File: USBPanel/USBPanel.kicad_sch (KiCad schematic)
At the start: 62 parts, among them J1 PORT1, J2 PORT2, J3 PWR, J4 USB_UFP, J5 SINK, J6 I2Ct, J7 I2Cc, Q1 ISZ0702NLS, Q2 ISZ0702NLS, Q3 NX138BK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

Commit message: USBPanel layout
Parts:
- added R18, R19: 4.7kΩ, Resistor_SMD:R_0603_1608Metric, symbol Device:R_US
- J7: symbol Connector_Generic:Conn_02x03_Top_Bottom -> Connector_Generic:Conn_02x03_Odd_Even
- R1, R2: value 2.2kΩ -> 4.7kΩ
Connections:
- net +3.3V: now also R18.1, R19.1
- net GND: now also J7.5 (Pin_5); no longer J7.3 (Pin_3)
- net PORT1_D+: now also U2.4 (I/O3); no longer U2.6 (I/O4)
- net PORT1_D-: now also U2.6 (I/O4); no longer U2.4 (I/O3)
- net at R1.1, U1.15 (I2Cc_SDA): now also J7.3 (Pin_3); no longer J7.5 (Pin_5)
- net at U3.5 (SDA): now also J7.4 (Pin_4), R19.2; no longer J7.2 (Pin_2)
- net at U3.6 (SCL): now also J7.2 (Pin_2), R18.2; no longer J7.1 (Pin_1)
- net at R2.1, U1.16 (I2Cc_SCL): now also J7.1 (Pin_1); no longer J7.4 (Pin_4)
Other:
- note added: "Jumper 1-2 and 3-4 for EEPROM patch loading"
- note removed: "Jumper 1-4 and 2-5 for EEPROM patch loading"

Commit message: USBPanel PCB complete
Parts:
- added C18: 10μF 50V, Capacitor_SMD:C_1206_3216Metric, symbol Device:C_Small
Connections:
- net GND: now also C18.2
- net PORT2_VBUS: now reaches C12.2, C13.2, D1.1 (A1), J2.A4 (VBUS), J2.A9 (VBUS), J2.B4 (VBUS), J2.B9 (VBUS), TP5.1, U4.14 (OUT), U4.15 (OUT)
- net PORT1_VBUS: now reaches C7.1, C8.1, J1.A4 (VBUS), J1.A9 (VBUS), J1.B4 (VBUS), J1.B9 (VBUS), Q1.1 (S), TP4.1, U1.26 (VBUS), U1.27 (VBUS), U2.5 (VBUS)
- net at J5.1 (Pin_1), Q2.1 (S), TP6.1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: now also C18.1
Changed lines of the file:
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@@
 	(wire
 		(pts
+			(xy 153.67 24.13) (xy 154.94 24.13)
+		)
+		(stroke
+			(width 0)
+			(type default)
+		)
+	)
+	(wire
+		(pts
 			(xy 233.68 52.07) (xy 264.16 52.07)
 		)
@@
 	(wire
 		(pts
+			(xy 154.94 24.13) (xy 154.94 26.67)
+		)
+		(stroke
+			(width 0)
+			(type default)
+		)
+	)
+	(wire
+		(pts
 			(xy 336.55 124.46) (xy 337.82 124.46)
 		)
@@
 	(wire
 		(pts
+			(xy 154.94 31.75) (xy 154.94 40.64)
+		)
+		(stroke
+			(width 0)
+			(type default)
+		)
+	)
+	(wire
+		(pts
 			(xy 71.12 128.27) (xy 72.39 128.27)
 		)
@@
 		)
 	)
+	(label "PORT2_VBUS"
+		(at 137.16 208.28 0)
+		(effects
+			(font
+				(size 1.27 1.27)
+			)
+			(justify left bottom)
+		)
+	)
 	(label "PORT1_UFP"
 		(at 189.23 81.28 0)
@@
 		)
 	)
+	(label "PORT1_VBUS"
+		(at 203.2 46.99 0)
+		(effects
+			(font
+				(size 1.27 1.27)
+			)
+			(justify left bottom)
+		)
+	)
 	(label "+3.3V_EXT"
 		(at 62.23 50.8 0)
@@
 					(unit 1)
 				)
+			)
+		)
+	)
+	(symbol
+		(lib_id "Device:C_Small")
+		(at 154.94 29.21 180)
+		(unit 1)
+		(exclude_from_sim no)
+		(in_bom yes)
+		(on_board yes)
+		(dnp yes)
+		(fields_autoplaced yes)
+		(property "Reference" "C18"
+			(at 157.48 27.9335 0)
+			(effects
+				(font
+					(size 1.27 1.27)
+				)
+				(justify right)
+			)
+		)
+		(property "Value" "10μF 50V"
+			(at 157.48 30.4735 0)
+			(effects
+				(font
+					(size 1.27 1.27)
+				)
+				(justify right)
+			)
+		)
+		(property "Footprint" "Capacitor_SMD:C_1206_3216Metric"
+			(at 154.94 29.21 0)
+			(effects
+				(font
+					(size 1.27 1.27)
+				)
+				(hide yes)
+			)
+		)
+		(property "Datasheet" "~"
+			(at 154.94 29.21 0)
+			(effects
+				(font
+					(size 1.27 1.27)
+				)
+				(hide yes)
+			)
+		)
+		(property "Description" "Unpolarized capacitor, small symbol"
+			(at 154.94 29.21 0)
+			(effects
+				(font
+					(size 1.27 1.27)
+				)
+				(hide yes)
+			)
+		)
+		(pin "2"
+		)
+		(pin "1"
+		)
+		(instances
+			(project "USBPanel"
+				(path "/f52a1888-27c7-4b9b-b7ad-ff7714476a26"
+					(reference "C18")
+					(unit 1)
+				)
+			)
+		)
+	)
+	(symbol
+		(lib_id "power:GND")
+		(at 153.67 24.13 270)
+		(unit 1)
+		(exclude_from_sim no)
+		(in_bom yes)
+		(on_board yes)
+		(dnp no)
+		(fields_autoplaced yes)
+		(property "Reference" "#PWR042"
+			(at 147.32 24.13 0)
+			(effects
+				(font
+					(size 1.27 1.27)
+				)
+				(hide yes)
+			)
+		)
+		(property "Value" "GND"
+			(at 149.86 24.1299 90)
+			(effects
+				(font
+					(size 1.27 1.27)
+				)
+				(justify right)
+			)
+		)
+		(property "Footprint" ""
+			(at 153.67 24.13 0)
+			(effects
+				(font
+					(size 1.27 1.27)
+				)
+				(hide yes)
+			)
+		)
+		(property "Datasheet" ""
+			(at 153.67 24.13 0)
+			(effects
+				(font
+					(size 1.27 1.27)
+				)
+				(hide yes)
+			)
+		)
+		(property "Description" "Power symbol creates a global label with name \"GND\" , ground"
+			(at 153.67 24.13 0)
+			(effects
+				(font
+					(size 1.27 1.27)
+				)
+				(hide yes)
+			)
+		)
+		(pin "1"
+		)
+		(instances
+			(project "USBPanel"
+				(path "/f52a1888-27c7-4b9b-b7ad-ff7714476a26"
+					(reference "#PWR042")
+					(unit 1)
+				)

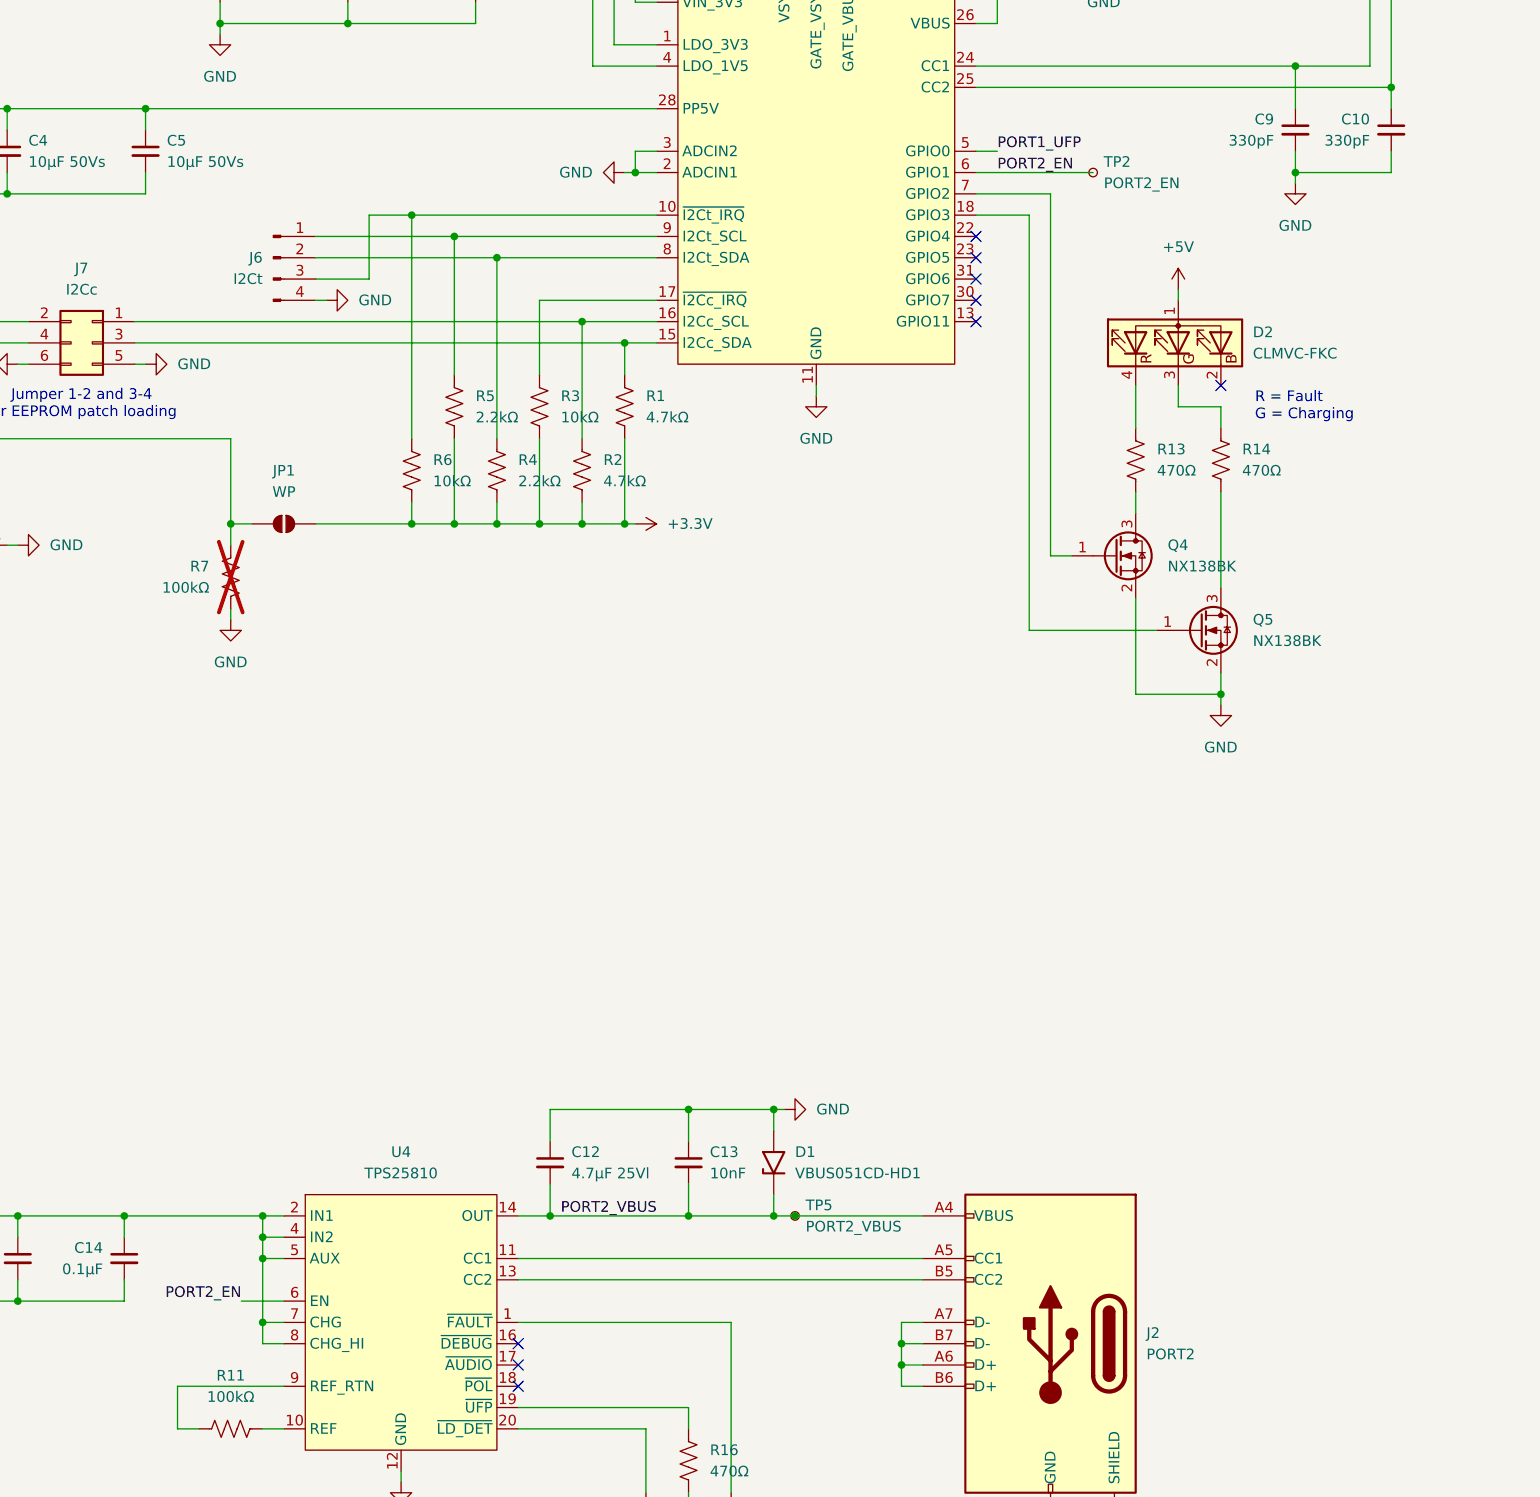
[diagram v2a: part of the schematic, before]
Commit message: USBPanel and I/O panel stuff ordered
Includes small changes and fixes for the USBPanel PCB, the main panel design itself, and various small parts for it
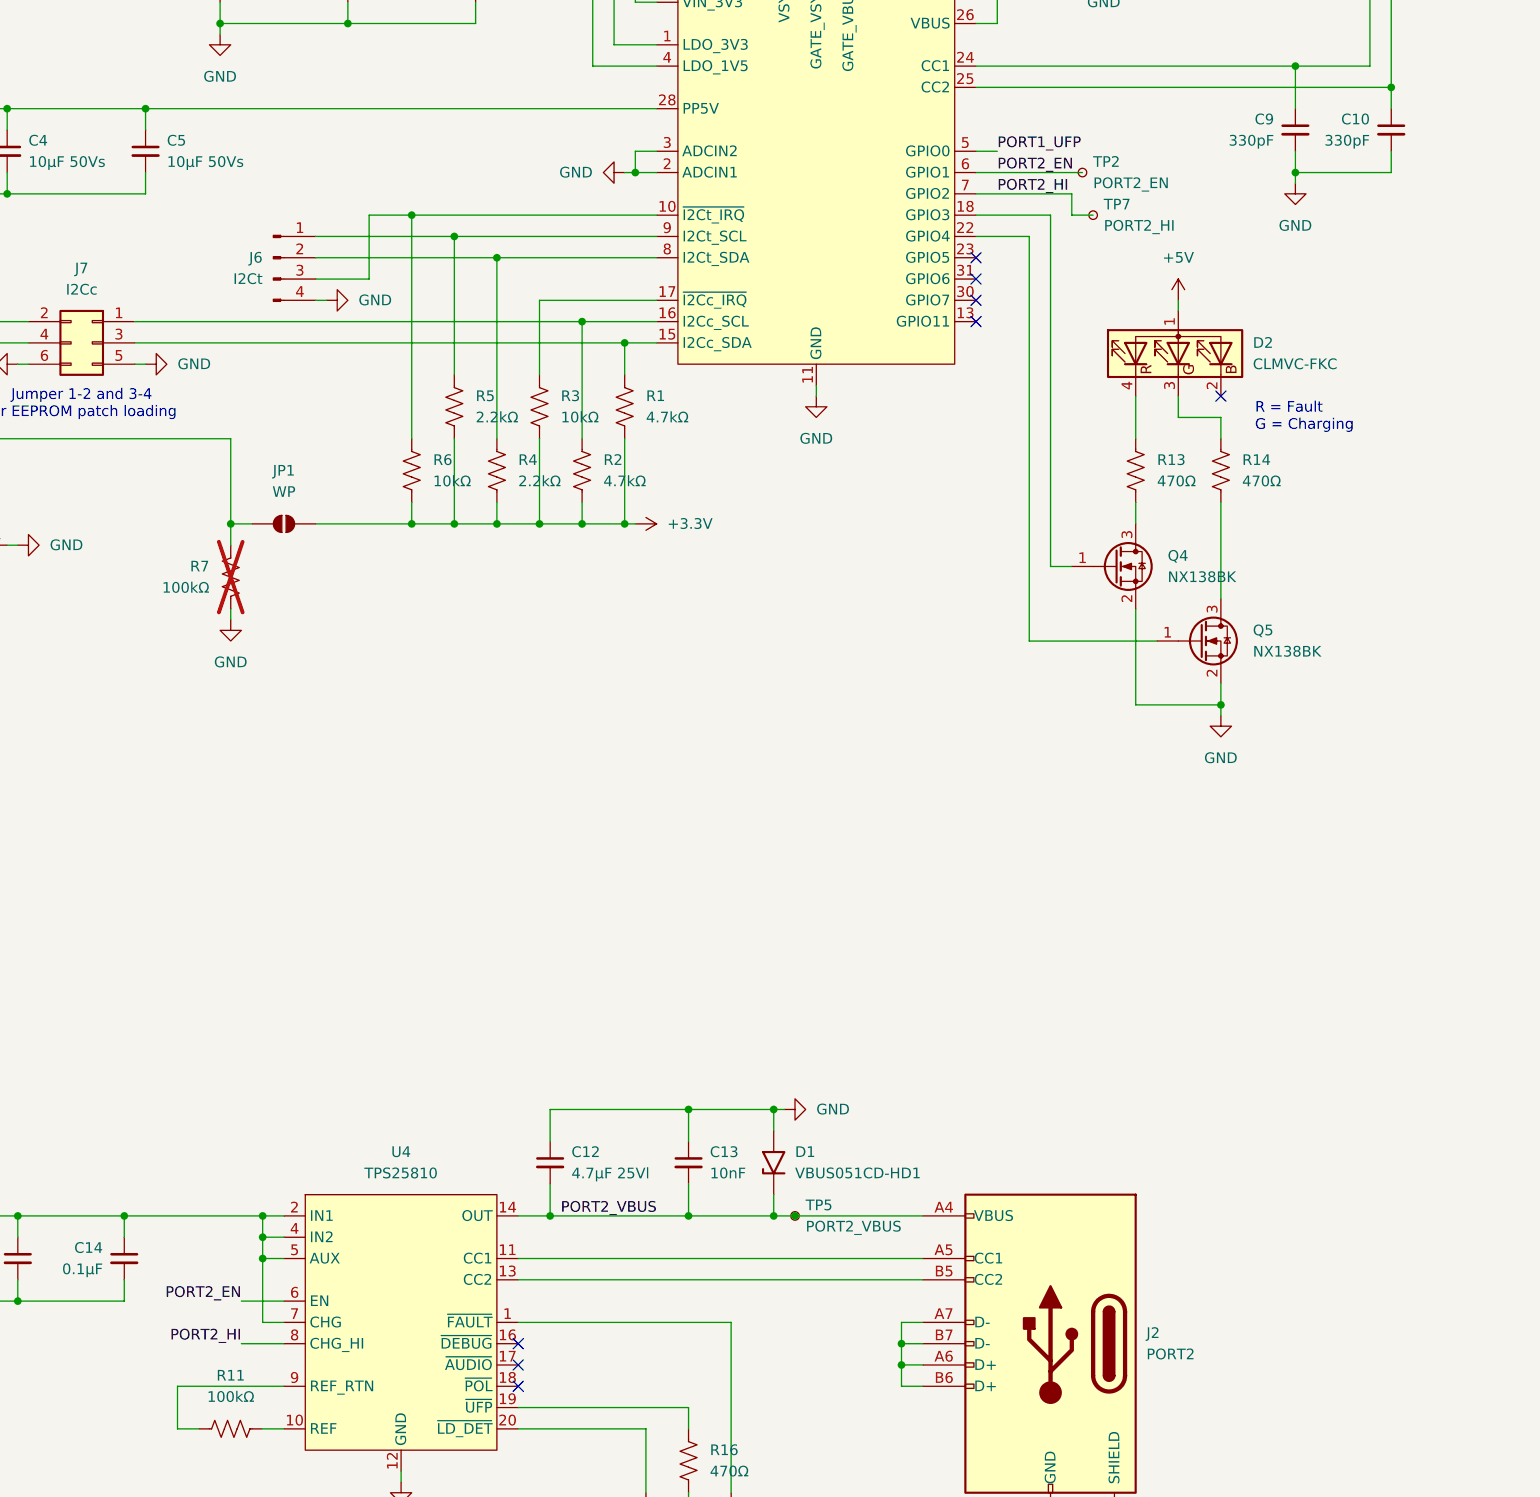
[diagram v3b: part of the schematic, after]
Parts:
- added TP7: PORT2_HI, BW_PassiveMechanical:TP_0603_1608Metric_Fused, symbol Connector:TestPoint_Small
- D2, D3: footprint LED_SMD:LED_Cree-PLCC4_2x2mm_CW -> BW_Active:LED_Cree-PLCC4_2x2mm_CW
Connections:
- net +5V: no longer U4.8 (CHG_HI)
- net at U1.18 (GPIO3): now also Q4.1 (G); no longer Q5.1 (G)
- net at U1.22 (GPIO4): now also Q5.1 (G)
- net PORT2_HI: now reaches U1.7 (GPIO2)
- net PORT2_HI: now also U4.8 (CHG_HI), TP7.1; no longer Q4.1 (G)
- no-connect marks 11 -> 10
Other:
- moved on the sheet: D2, Q4, Q5, R13, R14, TP2
